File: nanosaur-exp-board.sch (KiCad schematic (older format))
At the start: 4 parts, among them J1 jetson_nano, J2 Screw_Terminal_01x02, J3 nanosaur_exp, SW1 SW_DPDT_x2

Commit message: Fix layout board
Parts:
- J1: footprint Connector_PinHeader_2.54mm:PinHeader_2x20_P2.54mm_Vertical -> Connector_PinSocket_2.54mm:PinSocket_2x21_P2.54mm_Vertical
- J2: footprint TerminalBlock:TerminalBlock_Altech_AK300-2_P5.00mm -> TerminalBlock_4Ucon:TerminalBlock_4Ucon_1x02_P3.50mm_Horizontal
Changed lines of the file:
@@
 F 0 "J1" H 3900 3300 50  0000 L CNN
 F 1 "jetson_nano" H 3750 3400 50  0000 L CNN
-F 2 "Connector_PinHeader_2.54mm:PinHeader_2x20_P2.54mm_Vertical" H 3800 4250 50  0001 C CNN
+F 2 "Connector_PinSocket_2.54mm:PinSocket_2x21_P2.54mm_Vertical" H 3800 4250 50  0001 C CNN
 F 3 "" H 3800 4250 50  0001 C CNN
 	1    3550 4550
@@
 F 0 "J2" V 5550 1800 50  0000 R CNN
 F 1 "Screw_Terminal_01x02" V 5450 2150 50  0000 R CNN
-F 2 "TerminalBlock:TerminalBlock_Altech_AK300-2_P5.00mm" H 5300 1750 50  0001 C CNN
+F 2 "TerminalBlock_4Ucon:TerminalBlock_4Ucon_1x02_P3.50mm_Horizontal" H 5300 1750 50  0001 C CNN
 F 3 "~" H 5300 1750 50  0001 C CNN
 	1    5300 1750

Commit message: Exp improvements
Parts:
- added H1, H2, H3, H4: MountingHole, MountingHole:MountingHole_2.1mm, symbol Mechanical:MountingHole
- SW1: footprint Button_Switch_THT:SW_CuK_JS202011AQN_DPDT_Angled -> Button_Switch_THT:SW_E-Switch_EG1271_DPDT
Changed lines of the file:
@@
 F 0 "SW1" H 6150 2135 50  0000 C CNN
 F 1 "SW_DPDT_x2" H 6150 2044 50  0000 C CNN
-F 2 "Button_Switch_THT:SW_CuK_JS202011AQN_DPDT_Angled" H 6150 1850 50  0001 C CNN
+F 2 "Button_Switch_THT:SW_E-Switch_EG1271_DPDT" H 6150 1850 50  0001 C CNN
 F 3 "~" H 6150 1850 50  0001 C CNN
 	1    6150 1850
@@
 F 0 "SW1" H 6150 2685 50  0000 C CNN
 F 1 "SW_DPDT_x2" H 6150 2594 50  0000 C CNN
-F 2 "Button_Switch_THT:SW_CuK_JS202011AQN_DPDT_Angled" H 6150 2400 50  0001 C CNN
+F 2 "Button_Switch_THT:SW_E-Switch_EG1271_DPDT" H 6150 2400 50  0001 C CNN
 F 3 "~" H 6150 2400 50  0001 C CNN
 	2    6150 2400
@@
 NoConn ~ 6350 1750
 NoConn ~ 6350 2300
-NoConn ~ 2600 4750
-NoConn ~ 2600 4650
-NoConn ~ 2600 4550
+NoConn ~ 2600 5050
+NoConn ~ 2600 4950
+NoConn ~ 2600 4850
 NoConn ~ 2600 4450
 NoConn ~ 2600 4350
 Wire Wire Line
-	4150 3600 7400 3600
+	4450 3600 7400 3600
 Wire Wire Line
 	7400 3600 7400 3850
 Wire Wire Line
-	4150 3700 7300 3700
+	4450 3700 7300 3700
 Wire Wire Line
 	7300 3700 7300 3950
@@
 	7300 3950 7400 3950
 Wire Wire Line
-	4150 3900 7000 3900
+	4450 3900 7000 3900
 Wire Wire Line
 	7000 3900 7000 4150
@@
 	7000 4150 7400 4150
 Wire Wire Line
-	4150 4000 6900 4000
+	4450 4000 6900 4000
 Wire Wire Line
 	6900 4000 6900 4250
@@
 Wire Wire Line
 	5300 1950 5300 2100
+$Comp
+L Mechanical:MountingHole H1
+U 1 1 6045C837
+P 8750 1300
+F 0 "H1" H 8850 1346 50  0000 L CNN
+F 1 "MountingHole" H 8850 1255 50  0000 L CNN
+F 2 "MountingHole:MountingHole_2.1mm" H 8750 1300 50  0001 C CNN
+F 3 "~" H 8750 1300 50  0001 C CNN
+	1    8750 1300
+	1    0    0    -1
+$EndComp
+$Comp
+L Mechanical:MountingHole H2
+U 1 1 6045FDF6
+P 8750 1500
+F 0 "H2" H 8850 1546 50  0000 L CNN
+F 1 "MountingHole" H 8850 1455 50  0000 L CNN
+F 2 "MountingHole:MountingHole_2.1mm" H 8750 1500 50  0001 C CNN
+F 3 "~" H 8750 1500 50  0001 C CNN
+	1    8750 1500
+	1    0    0    -1
+$EndComp
+$Comp
+L Mechanical:MountingHole H3
+U 1 1 604606C8
+P 8750 1700
+F 0 "H3" H 8850 1746 50  0000 L CNN
+F 1 "MountingHole" H 8850 1655 50  0000 L CNN
+F 2 "MountingHole:MountingHole_2.1mm" H 8750 1700 50  0001 C CNN
+F 3 "~" H 8750 1700 50  0001 C CNN
+	1    8750 1700
+	1    0    0    -1
+$EndComp
+$Comp
+L Mechanical:MountingHole H4
+U 1 1 60460CF8
+P 8750 1900
+F 0 "H4" H 8850 1946 50  0000 L CNN
+F 1 "MountingHole" H 8850 1855 50  0000 L CNN
+F 2 "MountingHole:MountingHole_2.1mm" H 8750 1900 50  0001 C CNN
+F 3 "~" H 8750 1900 50  0001 C CNN
+	1    8750 1900
+	1    0    0    -1
+$EndComp
 $EndSCHEMATC

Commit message: Test actions
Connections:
- wire segments 33 -> 36
- no-connect marks 9 -> 21
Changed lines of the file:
@@
 	0    -1   -1   0
 $EndComp
-$Comp
-L power:+3V3 #PWR0107
-U 1 1 603E5A7B
-P 3500 3000
-F 0 "#PWR0107" H 3500 2850 50  0001 C CNN
-F 1 "+3V3" H 3515 3173 50  0000 C CNN
-F 2 "" H 3500 3000 50  0001 C CNN
-F 3 "" H 3500 3000 50  0001 C CNN
-	1    3500 3000
-	1    0    0    -1
-$EndComp
-$Comp
-L power:+3V3 #PWR0108
-U 1 1 603E5FD4
-P 3600 3000
-F 0 "#PWR0108" H 3600 2850 50  0001 C CNN
-F 1 "+3V3" H 3615 3173 50  0000 C CNN
-F 2 "" H 3600 3000 50  0001 C CNN
-F 3 "" H 3600 3000 50  0001 C CNN
-	1    3600 3000
-	1    0    0    -1
-$EndComp
-Wire Wire Line
-	3500 3000 3500 3150
-Wire Wire Line
-	3600 3000 3600 3150
 Wire Wire Line
 	2950 5750 3050 5750
@@
 Wire Wire Line
 	3350 6000 3350 5750
-$Comp
-L power:VCC #PWR0109
-U 1 1 603EF5FE
-P 3100 3000
-F 0 "#PWR0109" H 3100 2850 50  0001 C CNN
-F 1 "VCC" H 3115 3173 50  0000 C CNN
-F 2 "" H 3100 3000 50  0001 C CNN
-F 3 "" H 3100 3000 50  0001 C CNN
-	1    3100 3000
-	1    0    0    -1
-$EndComp
-$Comp
-L power:VCC #PWR0110
-U 1 1 603F0CBD
-P 3200 3000
-F 0 "#PWR0110" H 3200 2850 50  0001 C CNN
-F 1 "VCC" H 3215 3173 50  0000 C CNN
-F 2 "" H 3200 3000 50  0001 C CNN
-F 3 "" H 3200 3000 50  0001 C CNN
-	1    3200 3000
-	1    0    0    -1
-$EndComp
-Wire Wire Line
-	3100 3000 3100 3150
-Wire Wire Line
-	3200 3000 3200 3150
 Wire Wire Line
 	7400 4800 7200 4800
@@
 	1    0    0    -1
 $EndComp
+NoConn ~ 2600 4250
+NoConn ~ 2600 4150
+NoConn ~ 2600 4050
+NoConn ~ 2600 3900
+NoConn ~ 2600 3800
+NoConn ~ 4450 4200
+NoConn ~ 4450 4300
+NoConn ~ 4450 4400
+NoConn ~ 4450 4500
+NoConn ~ 4450 4600
+NoConn ~ 2600 4650
+NoConn ~ 2600 4750
+$Comp
+L power:PWR_FLAG #FLG0101
+U 1 1 6041593D
+P 1600 3400
+F 0 "#FLG0101" H 1600 3475 50  0001 C CNN
+F 1 "PWR_FLAG" H 1600 3573 50  0000 C CNN
+F 2 "" H 1600 3400 50  0001 C CNN
+F 3 "~" H 1600 3400 50  0001 C CNN
+	1    1600 3400
+	1    0    0    -1
+$EndComp
+$Comp
+L power:PWR_FLAG #FLG0102
+U 1 1 60416474
+P 2050 3400
+F 0 "#FLG0102" H 2050 3475 50  0001 C CNN
+F 1 "PWR_FLAG" H 2050 3573 50  0000 C CNN
+F 2 "" H 2050 3400 50  0001 C CNN
+F 3 "~" H 2050 3400 50  0001 C CNN
+	1    2050 3400
+	1    0    0    -1
+$EndComp
+$Comp
+L power:GND #PWR0107
+U 1 1 60416EF9
+P 2050 3600
+F 0 "#PWR0107" H 2050 3350 50  0001 C CNN
+F 1 "GND" H 2055 3427 50  0000 C CNN
+F 2 "" H 2050 3600 50  0001 C CNN
+F 3 "" H 2050 3600 50  0001 C CNN
+	1    2050 3600
+	1    0    0    -1
+$EndComp
+$Comp
+L power:VCC #PWR0108
+U 1 1 60417647
+P 1600 3600
+F 0 "#PWR0108" H 1600 3450 50  0001 C CNN
+F 1 "VCC" H 1615 3773 50  0000 C CNN
+F 2 "" H 1600 3600 50  0001 C CNN
+F 3 "" H 1600 3600 50  0001 C CNN
+	1    1600 3600
+	-1   0    0    1
+$EndComp
+Wire Wire Line
+	1600 3400 1600 3600
+Wire Wire Line
+	2050 3400 2050 3600
+$Comp
+L power:VCC #PWR0109
+U 1 1 6041C01D
+P 3100 2850
+F 0 "#PWR0109" H 3100 2700 50  0001 C CNN
+F 1 "VCC" H 3115 3023 50  0000 C CNN
+F 2 "" H 3100 2850 50  0001 C CNN
+F 3 "" H 3100 2850 50  0001 C CNN
+	1    3100 2850
+	1    0    0    -1
+$EndComp
+$Comp
+L power:VCC #PWR0110
+U 1 1 6041C9F0
+P 3200 2850
+F 0 "#PWR0110" H 3200 2700 50  0001 C CNN
+F 1 "VCC" H 3215 3023 50  0000 C CNN
+F 2 "" H 3200 2850 50  0001 C CNN
+F 3 "" H 3200 2850 50  0001 C CNN
+	1    3200 2850
+	1    0    0    -1
+$EndComp
+$Comp
+L power:+3V3 #PWR0111
+U 1 1 6041DCFE
+P 3500 2850
+F 0 "#PWR0111" H 3500 2700 50  0001 C CNN
+F 1 "+3V3" H 3515 3023 50  0000 C CNN
+F 2 "" H 3500 2850 50  0001 C CNN
+F 3 "" H 3500 2850 50  0001 C CNN
+	1    3500 2850
+	1    0    0    -1
+$EndComp
+$Comp
+L power:+3V3 #PWR0112
+U 1 1 6041E566
+P 3600 2850
+F 0 "#PWR0112" H 3600 2700 50  0001 C CNN
+F 1 "+3V3" H 3615 3023 50  0000 C CNN
+F 2 "" H 3600 2850 50  0001 C CNN
+F 3 "" H 3600 2850 50  0001 C CNN
+	1    3600 2850
+	1    0    0    -1
+$EndComp
+Wire Wire Line
+	3100 2850 3100 3150
+Wire Wire Line
+	3200 2850 3200 3150
+Wire Wire Line
+	3500 2850 3500 3150
+Wire Wire Line
+	3600 2850 3600 3150
+$Comp
+L power:PWR_FLAG #FLG0103
+U 1 1 60421B20
+P 1300 3400
+F 0 "#FLG0103" H 1300 3475 50  0001 C CNN
+F 1 "PWR_FLAG" H 1300 3573 50  0000 C CNN
+F 2 "" H 1300 3400 50  0001 C CNN
+F 3 "~" H 1300 3400 50  0001 C CNN
+	1    1300 3400
+	1    0    0    -1
+$EndComp
+$Comp
+L power:+3V3 #PWR0113
+U 1 1 604220AE
+P 1300 3650
+F 0 "#PWR0113" H 1300 3500 50  0001 C CNN
+F 1 "+3V3" H 1315 3823 50  0000 C CNN
+F 2 "" H 1300 3650 50  0001 C CNN
+F 3 "" H 1300 3650 50  0001 C CNN
+	1    1300 3650
+	-1   0    0    1
+$EndComp
+Wire Wire Line
+	1300 3400 1300 3650
 $EndSCHEMATC

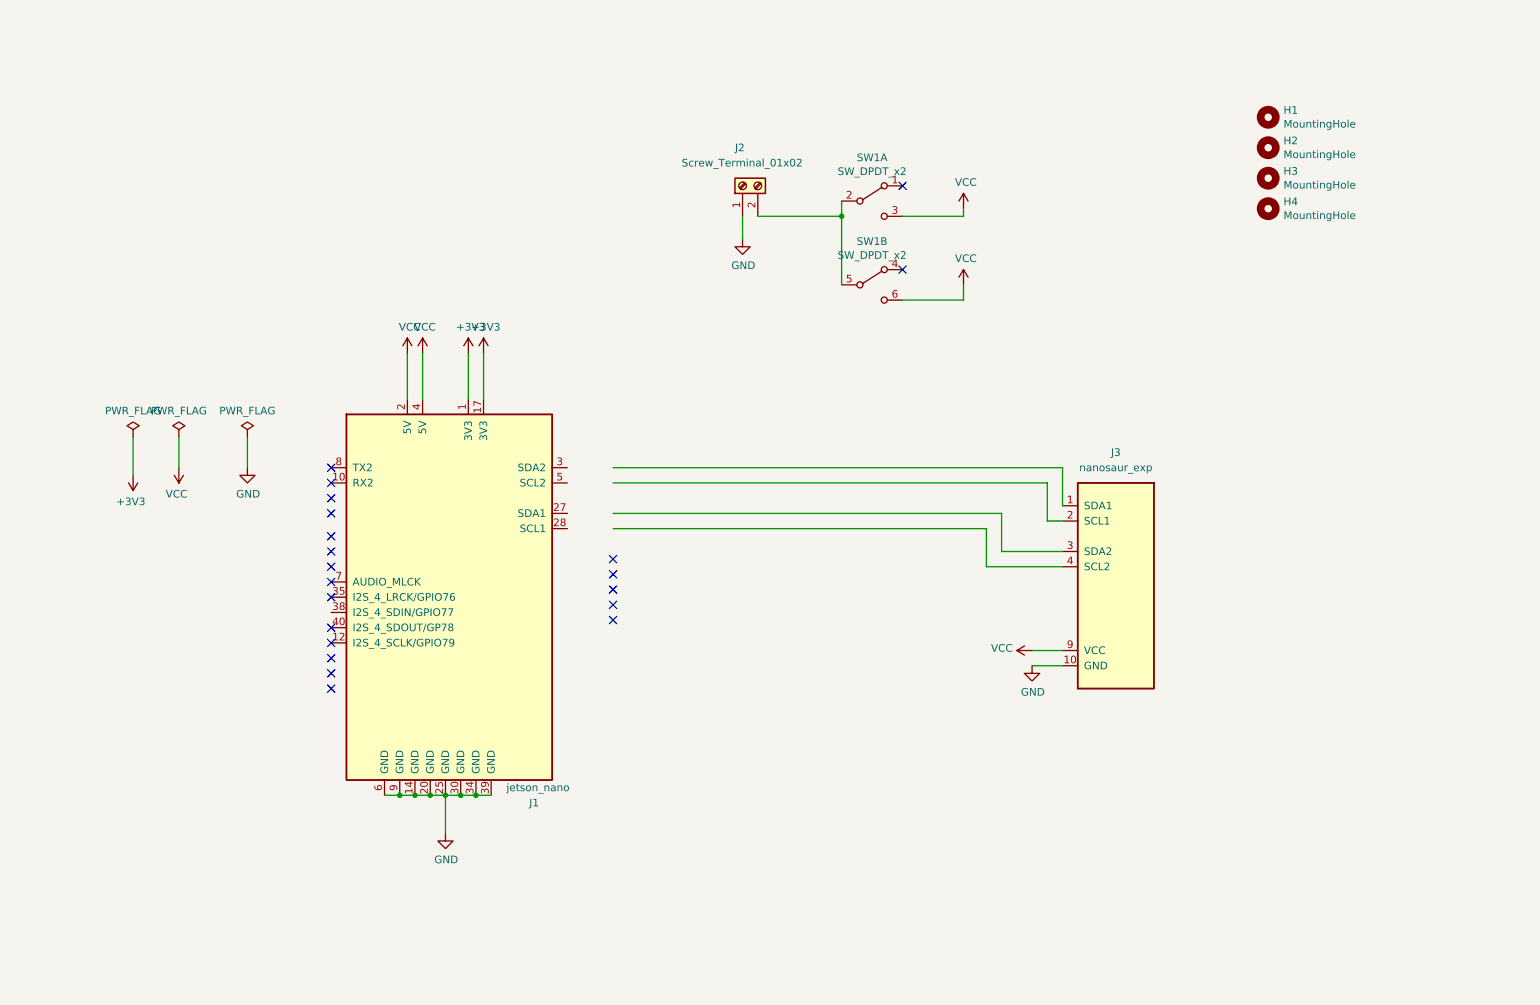
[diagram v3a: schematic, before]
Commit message: Added first rev of exp board
Added first revision of the expansion Board.

Note ! Board is work in progress.
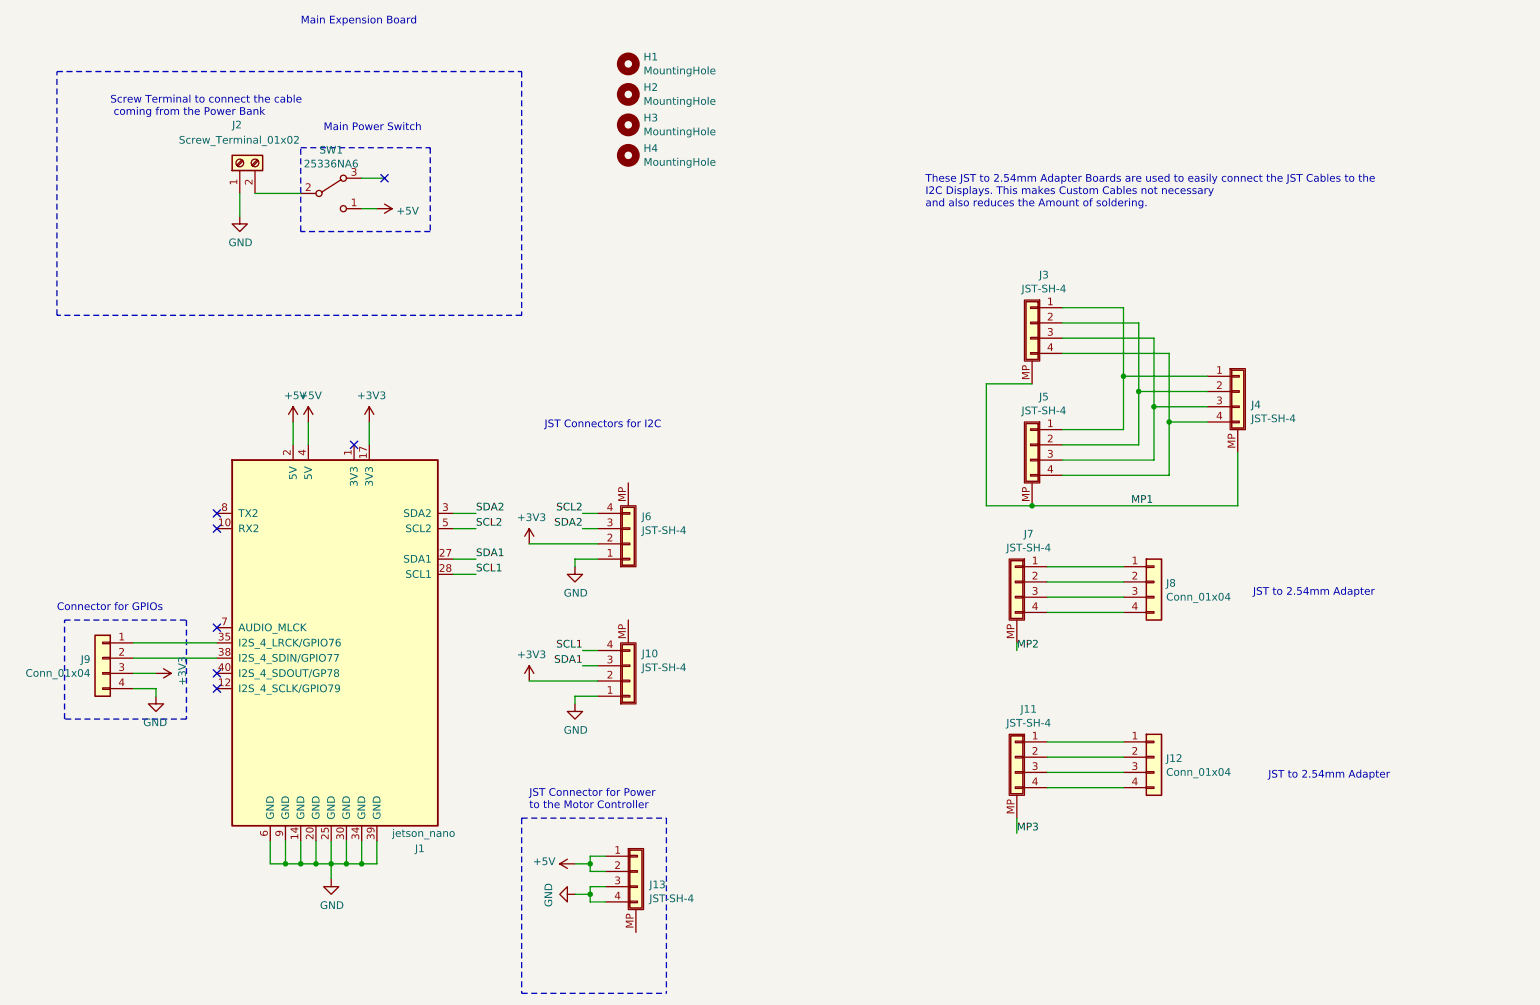
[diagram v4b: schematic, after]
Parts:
- removed J3: nanosaur_exp, Connector_PinSocket_2.54mm:PinSocket_1x10_P2.54mm_Vertical, symbol nanosaur:nanosaur_exp
- removed SW1: SW_DPDT_x2, Button_Switch_THT:SW_E-Switch_EG1271_DPDT, symbol Switch:SW_DPDT_x2
- added J10, J11, J13, J3, J4, J5, J6, J7: JST-SH-4, Connector_JST:JST_SH_SM04B-SRSS-TB_1x04-1MP_P1.00mm_Horizontal, symbol JST-SH-4:JST-SH-4
- added J12, J8: Conn_01x04, Connector_PinSocket_2.54mm:PinSocket_1x04_P2.54mm_Vertical, symbol Connector_Generic:Conn_01x04
- added J9: Conn_01x04, Connector_PinHeader_2.54mm:PinHeader_1x04_P2.54mm_Vertical, symbol Connector_Generic:Conn_01x04
- added SW1: 25336NA6, SamacSys_Parts:25336NA6, symbol 25336NA6:25336NA6
- J1: footprint Connector_PinSocket_2.54mm:PinSocket_2x21_P2.54mm_Vertical -> Connector_PinHeader_2.54mm:PinHeader_2x20_P2.54mm_Vertical
- J2: footprint TerminalBlock_4Ucon:TerminalBlock_4Ucon_1x02_P3.50mm_Horizontal -> TerminalBlock:TerminalBlock_Altech_AK300-2_P5.00mm
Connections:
- net labels added: +5V, MP1, MP2, MP3, SCL1, SCL2, SDA1, SDA2
- net labels removed: VCC
- wire segments 36 -> 87
- no-connect marks 21 -> 7
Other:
- note added: "Connector for GPIOs"
- note added: "JST Connector for Power\nto the Motor Controller"
- note added: "JST Connectors for I2C"
- note added: "JST to 2.54mm Adapter\n"
- note added: "Main Expension Board"
- note added: "Main Power Switch"
- note added: "Screw Terminal to connect the cable\n coming from the Power Bank"
- note added: "These JST to 2.54mm Adapter Boards are used to easily connect the JST Cables to the\nI2C Displays. This makes Custom Cables not necessary\nand also reduces the Amount of soldering."
- moved on the sheet: J1, J2
